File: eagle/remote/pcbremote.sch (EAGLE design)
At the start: 39 parts, among them CN1 SOCKET 1x2, IC1 MCP73831/OT, J1 FEMALE 1x2, J2 455-1750-1-ND, J4 FEMALE 2x4, J5 FEMALE 2x3, J6 455-1750-1-ND, Q1 FDC638P, U1 LTC1540CS8PBF, U2 LTC4412ES6TRPBF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

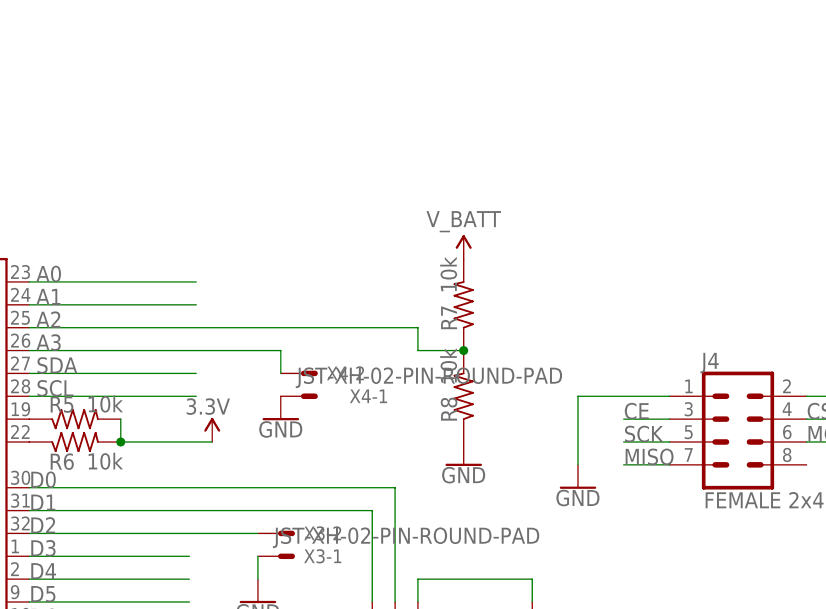
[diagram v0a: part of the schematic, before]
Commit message: Update Hall 3 pin
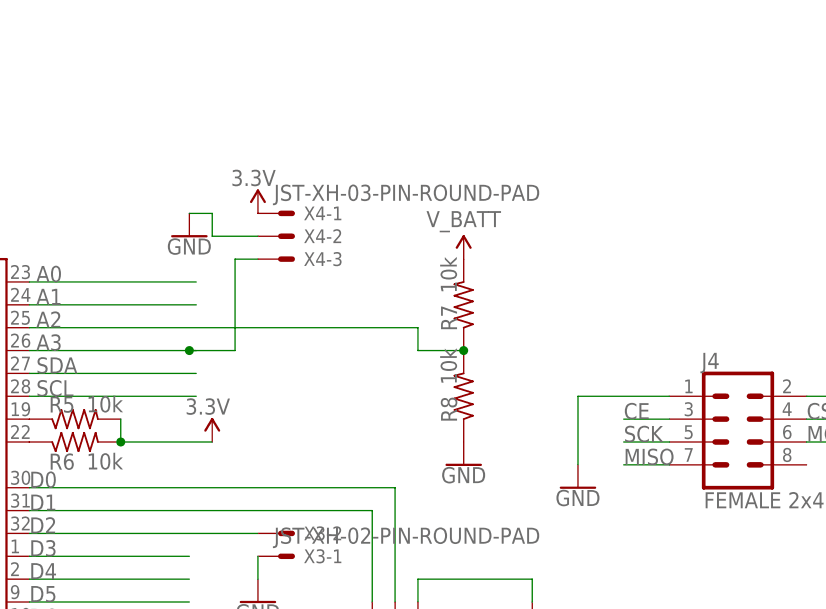
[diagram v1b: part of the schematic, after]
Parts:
- X4: value JST-XH-02-PIN-ROUND-PAD -> JST-XH-03-PIN-ROUND-PAD; device Rembrandt Electronics - JST XH Connectors v1-0:JST-XH-02-PIN-ROUND-PAD -> Rembrandt Electronics - JST XH Connectors v1-0:JST-XH-03-PIN-ROUND-PAD
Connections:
- net 3.3V: now also X4-1.S
- net A3: now also X4-3.S; no longer X4-2.S
- net GND: now also X4-2.S; no longer X4-1.S
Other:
- moved on the sheet: X4-1, X4-2
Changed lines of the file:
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@@
 <part name="X3" library="Rembrandt Electronics - JST XH Connectors v1-0" deviceset="JST-XH-02-PIN" device="-ROUND-PAD"/>
 <part name="GND19" library="SparkFun-PowerSymbols" deviceset="GND" device=""/>
-<part name="X4" library="Rembrandt Electronics - JST XH Connectors v1-0" deviceset="JST-XH-02-PIN" device="-ROUND-PAD"/>
-<part name="GND20" library="SparkFun-PowerSymbols" deviceset="GND" device=""/>
 <part name="J6" library="SparkFun-Connectors" deviceset="CONN_03" device="" value="455-1750-1-ND"/>
 <part name="GND21" library="SparkFun-PowerSymbols" deviceset="GND" device=""/>
@@
 <part name="GND22" library="SparkFun-PowerSymbols" deviceset="GND" device=""/>
 <part name="GND23" library="SparkFun-PowerSymbols" deviceset="GND" device=""/>
+<part name="X4" library="Rembrandt Electronics - JST XH Connectors v1-0" deviceset="JST-XH-03-PIN" device="-ROUND-PAD"/>
+<part name="SUPPLY12" library="SparkFun-PowerSymbols" deviceset="3.3V" device=""/>
+<part name="GND20" library="SparkFun-PowerSymbols" deviceset="GND" device=""/>
 </parts>
 <sheets>
@@
 <attribute name="VALUE" x="297.18" y="149.606" size="1.778" layer="96" align="top-center"/>
 </instance>
-<instance part="X4" gate="-2" x="302.26" y="175.26" smashed="yes">
-<attribute name="NAME" x="304.8" y="174.498" size="1.524" layer="95"/>
-</instance>
-<instance part="X4" gate="-1" x="302.26" y="172.72" smashed="yes">
-<attribute name="NAME" x="307.34" y="171.958" size="1.524" layer="95"/>
-<attribute name="VALUE" x="301.498" y="174.117" size="1.778" layer="96"/>
-</instance>
-<instance part="GND20" gate="1" x="299.72" y="170.18" smashed="yes">
-<attribute name="VALUE" x="299.72" y="169.926" size="1.778" layer="96" align="top-center"/>
-</instance>
 <instance part="J6" gate="J$1" x="312.42" y="142.24" smashed="yes" rot="R90">
 <attribute name="VALUE" x="322.326" y="132.08" size="1.778" layer="96" font="vector" rot="R90"/>
@@
 <instance part="GND23" gate="1" x="335.28" y="124.46" smashed="yes" rot="R270">
 <attribute name="VALUE" x="335.026" y="124.46" size="1.778" layer="96" rot="R270" align="top-center"/>
+</instance>
+<instance part="X4" gate="-1" x="299.72" y="193.04" smashed="yes">
+<attribute name="NAME" x="302.26" y="192.278" size="1.524" layer="95"/>
+<attribute name="VALUE" x="298.958" y="194.437" size="1.778" layer="96"/>
+</instance>
+<instance part="X4" gate="-2" x="299.72" y="190.5" smashed="yes">
+<attribute name="NAME" x="302.26" y="189.738" size="1.524" layer="95"/>
+</instance>
+<instance part="X4" gate="-3" x="299.72" y="187.96" smashed="yes">
+<attribute name="NAME" x="302.26" y="187.198" size="1.524" layer="95"/>
+</instance>
+<instance part="SUPPLY12" gate="G$1" x="297.18" y="193.04" smashed="yes" rot="MR0">
+<attribute name="VALUE" x="296.672" y="196.088" size="1.778" layer="96" rot="MR0" align="bottom-center"/>
+</instance>
+<instance part="GND20" gate="1" x="289.56" y="190.5" smashed="yes">
+<attribute name="VALUE" x="289.56" y="190.246" size="1.778" layer="96" align="top-center"/>
 </instance>
 </instances>
@@
 </segment>
 <segment>
-<pinref part="X4" gate="-1" pin="S"/>
-<pinref part="GND20" gate="1" pin="GND"/>
-</segment>
-<segment>
 <pinref part="X3" gate="-1" pin="S"/>
 <pinref part="GND19" gate="1" pin="GND"/>
@@
 <pinref part="X6" gate="-1" pin="S"/>
 <pinref part="GND23" gate="1" pin="GND"/>
+</segment>
+<segment>
+<pinref part="GND20" gate="1" pin="GND"/>
+<wire x1="289.56" y1="193.04" x2="292.1" y2="193.04" width="0.1524" layer="91"/>
+<wire x1="292.1" y1="193.04" x2="292.1" y2="190.5" width="0.1524" layer="91"/>
+<pinref part="X4" gate="-2" pin="S"/>
+<wire x1="292.1" y1="190.5" x2="297.18" y2="190.5" width="0.1524" layer="91"/>
 </segment>
 </net>
@@
 <wire x1="66.04" y1="132.08" x2="60.96" y2="132.08" width="0.1524" layer="91"/>
 </segment>
+<segment>
+<pinref part="X4" gate="-1" pin="S"/>
+<pinref part="SUPPLY12" gate="G$1" pin="3.3V"/>
+</segment>
 </net>
 <net name="MISO" class="0">
@@
 <label x="272.542" y="177.8" size="1.778" layer="95" grouprefs="ATMEGA328P"/>
 <pinref part="U4" gate="U1" pin="PC3(ADC3)"/>
-<pinref part="X4" gate="-2" pin="S"/>
 <wire x1="289.56" y1="177.8" x2="290.322" y2="177.8" width="0.1524" layer="91" grouprefs="ATMEGA328P"/>
-<wire x1="299.72" y1="175.26" x2="299.72" y2="177.8" width="0.1524" layer="91"/>
-<wire x1="299.72" y1="177.8" x2="290.322" y2="177.8" width="0.1524" layer="91"/>
-</segment>
-</net>
+<wire x1="289.56" y1="177.8" x2="294.64" y2="177.8" width="0.1524" layer="91"/>
+<junction x="289.56" y="177.8"/>
+<pinref part="X4" gate="-3" pin="S"/>
+<wire x1="297.18" y1="187.96" x2="294.64" y2="187.96" width="0.1524" layer="91"/>
+<wire x1="294.64" y1="187.96" x2="294.64" y2="177.8" width="0.1524" layer="91"/>
+</segment>
+</net>

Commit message: Remote almost finish
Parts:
- removed CN1: SOCKET 1x2, adafruit:JST_2PIN-THM
- removed J6: 455-1750-1-ND, SparkFun-Connectors:CONN_03
- removed X2, X3, X5, X6: JST-XH-02-PIN-ROUND-PAD, Rembrandt Electronics - JST XH Connectors v1-0:JST-XH-02-PIN-ROUND-PAD
- added BATT: SOCKET 1x2, adafruit:JST_2PIN-THM
- added BUTTONS, CHARGE, LED: JST-XH-03-PIN-ROUND-PAD, Rembrandt Electronics - JST XH Connectors v1-0:JST-XH-03-PIN-ROUND-PAD
- added R10, R11, R9: 470, rcl:R-US_R0805
- renumbered J1 to USB, J2 to SW, J4 to NRF, J5 to PROG, X1 to OLED, X4 to HALL
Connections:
- new net N$2: CHARGE-1.S, R9.2
- net D0: no longer J6.2
- net D1: no longer J6.3
- net D2: now also BUTTONS-1.S; no longer X3-2.S
- net D3: now also BUTTONS-2.S; no longer X5-2.S
- net D4: now also LED-1.S, R11.1; no longer X6-2.S
- net D5: now also LED-2.S, R10.1
- net GND: now also BATT.1, BUTTONS-3.S, LED-3.S, R10.2, R11.2, R9.1; no longer CN1.2, J6.1, X3-1.S, X5-1.S, X6-1.S
- net N$10: now also BATT.2; no longer CN1.1
- net N$5: now also CHARGE-2.S; no longer X2-1.S
- net V_USB: now also CHARGE-3.S; no longer X2-2.S
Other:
- note added: "Buttons"
- note added: "HALL"
